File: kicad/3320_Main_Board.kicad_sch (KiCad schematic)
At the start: 53 parts, among them J5 EuroPower_JST_3P, J6 EURO_PWR_16P, U1 AS3320, U2 TL072, U3 TL074

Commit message: added pcb rev 0.1.0
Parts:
- R1, R10, R11, R12, R13, R14, R15, R16, R17, R18, R19, R2, R20, R21, R22, R23, R24, R25, R26, R27, R28, R29, R3, R30, R31, R4, R5, R6, R7, R8, R9: footprint DIYSynthMNL:R_quarter_watt_L6.3mm_D2.5mm_P7.62mm -> Resistor_THT:R_Axial_DIN0207_L6.3mm_D2.5mm_P2.54mm_Vertical

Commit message: updated pcb revision 0.1.0
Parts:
- added H1: MountingHole_Pad, DIYSynthMNL:MountingHole_M3_Standoff_Pad, symbol Mechanical:MountingHole_Pad
- C12, C9: footprint DIYSynthMNL:CP_Radial_D4.0mm_P1.50mm -> DIYSynthMNL:CP_Radial_D5.0mm_P2.50mm
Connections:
- net GND: now also H1.1
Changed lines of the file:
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@@
       (effects (font (size 1.27 1.27)) (justify left))
     )
-    (property "Footprint" "DIYSynthMNL:CP_Radial_D4.0mm_P1.50mm" (at 117.1702 262.89 0)
+    (property "Footprint" "DIYSynthMNL:CP_Radial_D5.0mm_P2.50mm" (at 117.1702 262.89 0)
       (effects (font (size 1.27 1.27)) hide)
     )
@@
         (path "/03f11930-f7c0-4ced-9742-79790ca3496b/6be4c3d1-05b5-4b24-bcf9-a639c6a20d54"
           (reference "R25") (unit 1)
+        )
+      )
+    )
+  )
+  (symbol (lib_id "Mechanical:MountingHole_Pad") (at 285.75 228.6 0) (unit 1)
+    (in_bom yes) (on_board yes) (dnp no) (fields_autoplaced)
+    (property "Reference" "H1" (at 288.29 226.06 0)
+      (effects (font (size 1.27 1.27)) (justify left))
+    )
+    (property "Value" "MountingHole_Pad" (at 288.29 228.6 0)
+      (effects (font (size 1.27 1.27)) (justify left))
+    )
+    (property "Footprint" "DIYSynthMNL:MountingHole_M3_Standoff_Pad" (at 285.75 228.6 0)
+      (effects (font (size 1.27 1.27)) hide)
+    )
+    (property "Datasheet" "~" (at 285.75 228.6 0)
+      (effects (font (size 1.27 1.27)) hide)
+    )
+    (pin "1")
+    (instances
+      (project "3320-VCF"
+        (path "/03f11930-f7c0-4ced-9742-79790ca3496b/6be4c3d1-05b5-4b24-bcf9-a639c6a20d54"
+          (reference "H1") (unit 1)
         )
       )
@@
       (effects (font (size 1.27 1.27)) (justify left))
     )
-    (property "Footprint" "DIYSynthMNL:CP_Radial_D4.0mm_P1.50mm" (at 117.1702 255.27 0)
+    (property "Footprint" "DIYSynthMNL:CP_Radial_D5.0mm_P2.50mm" (at 117.1702 255.27 0)
       (effects (font (size 1.27 1.27)) hide)
     )
@@
         )
       )
+      (project "Electric Druid VCDO1"
+        (path "/1a79e409-2950-446e-9b6e-16f6bf0a888d/940513db-8445-4e70-8397-130f22045b59"
+          (reference "#PWR?") (unit 1)
+        )
+        (path "/1a79e409-2950-446e-9b6e-16f6bf0a888d"
+          (reference "#PWR?") (unit 1)
+        )
+      )
+      (project "3340-VCO"
+        (path "/aedb3b78-1db1-4bb8-b4e7-c509f764608a"
+          (reference "#PWR?") (unit 1)
+        )
+      )
+    )
+  )
+  (symbol (lib_id "power:GND") (at 285.75 231.14 0) (unit 1)
+    (in_bom yes) (on_board yes) (dnp no) (fields_autoplaced)
+    (property "Reference" "#PWR034" (at 285.75 237.49 0)
+      (effects (font (size 1.27 1.27)) hide)
+    )
+    (property "Value" "GND" (at 285.75 235.585 0)
+      (effects (font (size 1.27 1.27)))
+    )
+    (property "Footprint" "" (at 285.75 231.14 0)
+      (effects (font (size 1.27 1.27)) hide)
+    )
+    (property "Datasheet" "" (at 285.75 231.14 0)
+      (effects (font (size 1.27 1.27)) hide)
+    )
+    (pin "1")
+    (instances
+      (project "3320-VCF"
+        (path "/03f11930-f7c0-4ced-9742-79790ca3496b"
+          (reference "#PWR034") (unit 1)
+        )
+        (path "/03f11930-f7c0-4ced-9742-79790ca3496b/6be4c3d1-05b5-4b24-bcf9-a639c6a20d54"
+          (reference "#PWR01") (unit 1)
+        )
+      )

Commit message: updated pcb rev 0.1.0
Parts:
- U1: footprint DIYSynthMNL:DIP-18_W7.62mm_LongPads -> Package_DIP:DIP-18_W7.62mm_Socket_LongPads
- U2: footprint DIYSynthMNL:DIP-8_W7.62mm_LongPads -> Package_DIP:DIP-8_W7.62mm_Socket_LongPads
- U3: footprint DIYSynthMNL:DIP-14_W7.62mm_LongPads -> Package_DIP:DIP-14_W7.62mm_Socket_LongPads
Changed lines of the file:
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@@
       (effects (font (size 1.27 1.27)))
     )
-    (property "Footprint" "DIYSynthMNL:DIP-8_W7.62mm_LongPads" (at 295.8592 65.024 0)
+    (property "Footprint" "Package_DIP:DIP-8_W7.62mm_Socket_LongPads" (at 295.8592 65.024 0)
       (effects (font (size 1.27 1.27)) hide)
     )
@@
       (effects (font (size 1.27 1.27)))
     )
-    (property "Footprint" "DIYSynthMNL:DIP-14_W7.62mm_LongPads" (at 89.8652 207.3148 0)
+    (property "Footprint" "Package_DIP:DIP-14_W7.62mm_Socket_LongPads" (at 89.8652 207.3148 0)
       (effects (font (size 1.27 1.27)) hide)
     )
@@
       (effects (font (size 1.27 1.27)))
     )
-    (property "Footprint" "DIYSynthMNL:DIP-14_W7.62mm_LongPads" (at 200.9902 263.652 0)
+    (property "Footprint" "Package_DIP:DIP-14_W7.62mm_Socket_LongPads" (at 200.9902 263.652 0)
       (effects (font (size 1.27 1.27)) hide)
     )
@@
       (effects (font (size 1.27 1.27)))
     )
-    (property "Footprint" "DIYSynthMNL:DIP-8_W7.62mm_LongPads" (at 137.1092 62.484 0)
+    (property "Footprint" "Package_DIP:DIP-8_W7.62mm_Socket_LongPads" (at 137.1092 62.484 0)
       (effects (font (size 1.27 1.27)) hide)
     )
@@
       (effects (font (size 1.27 1.27)))
     )
-    (property "Footprint" "DIYSynthMNL:DIP-18_W7.62mm_LongPads" (at 194.2592 125.73 0)
+    (property "Footprint" "Package_DIP:DIP-18_W7.62mm_Socket_LongPads" (at 194.2592 125.73 0)
       (effects (font (size 1.27 1.27)) hide)
     )
@@
       (effects (font (size 1.27 1.27)) (justify left))
     )
-    (property "Footprint" "DIYSynthMNL:DIP-14_W7.62mm_LongPads" (at 148.0312 250.317 0)
+    (property "Footprint" "Package_DIP:DIP-14_W7.62mm_Socket_LongPads" (at 148.0312 250.317 0)
       (effects (font (size 1.27 1.27)) hide)
     )
@@
       (effects (font (size 1.27 1.27)) (justify left))
     )
-    (property "Footprint" "DIYSynthMNL:DIP-8_W7.62mm_LongPads" (at 138.3792 252.857 0)
+    (property "Footprint" "Package_DIP:DIP-8_W7.62mm_Socket_LongPads" (at 138.3792 252.857 0)
       (effects (font (size 1.27 1.27)) hide)
     )
@@
       (effects (font (size 1.27 1.27)))
     )
-    (property "Footprint" "DIYSynthMNL:DIP-14_W7.62mm_LongPads" (at 61.1632 204.7748 0)
+    (property "Footprint" "Package_DIP:DIP-14_W7.62mm_Socket_LongPads" (at 61.1632 204.7748 0)
       (effects (font (size 1.27 1.27)) hide)
     )
@@
       (effects (font (size 1.27 1.27)))
     )
-    (property "Footprint" "DIYSynthMNL:DIP-14_W7.62mm_LongPads" (at 70.6628 148.2852 0)
-      (effects (font (size 1.27 1.27)) hide)
-    )
+    (property "Footprint" "Package_DIP:DIP-14_W7.62mm_Socket_LongPads" (at 70.6628 148.2852 0)
+      (effects (font (size 1.27 1.27)) hide)
+    )

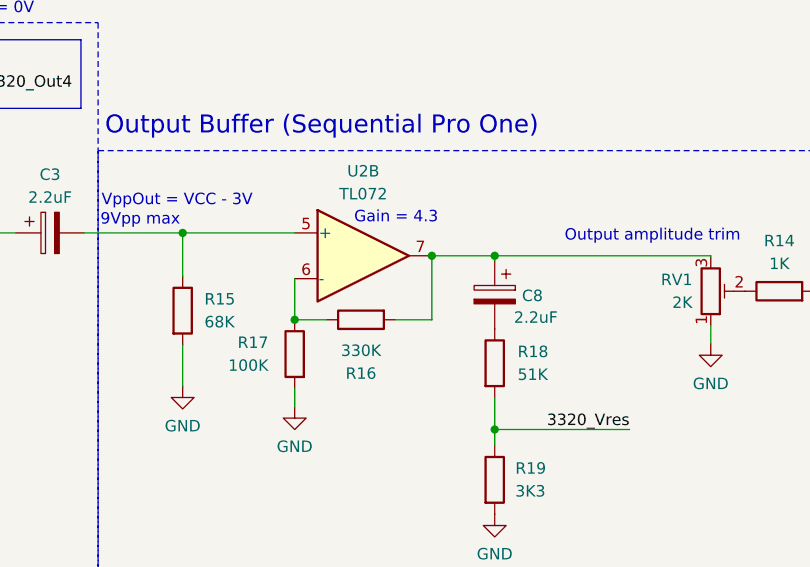
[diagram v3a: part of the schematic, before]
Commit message: Add schematic revision 0.1.5
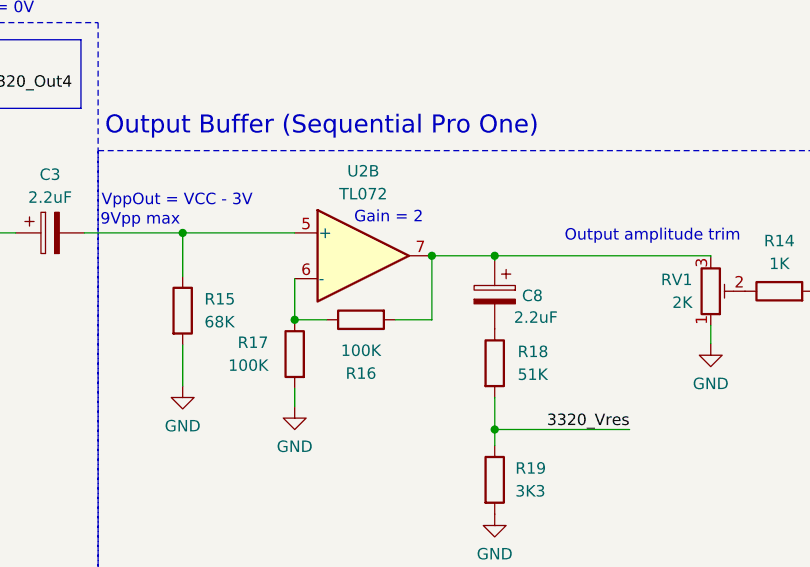
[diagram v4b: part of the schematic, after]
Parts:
- R16: value 330K -> 100K
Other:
- note added: "Gain = 2"
- note removed: "Gain = 4.3"
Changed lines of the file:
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@@
     (title "Eurorack 3320 Low Pass VCF")
     (date "2024-02-16")
-    (rev "0.1.4")
+    (rev "0.1.5")
     (company "DIYSynthMNL")
     (comment 1 "This version is a prototype")
@@
     (effects (font (size 1.27 1.27)) (justify left bottom))
   )
-  (text "Gain = 4.3" (at 294.8432 61.595 0)
+  (text "Gain = 2\n" (at 294.8432 61.595 0)
     (effects (font (size 1.27 1.27)) (justify left bottom))
   )
@@
       (effects (font (size 1.27 1.27)))
     )
-    (property "Value" "330K" (at 295.6052 75.565 90)
-      (effects (font (size 1.27 1.27)))
-    )
+    (property "Value" "100K" (at 295.6052 75.565 90)
+      (effects (font (size 1.27 1.27)))
+    )

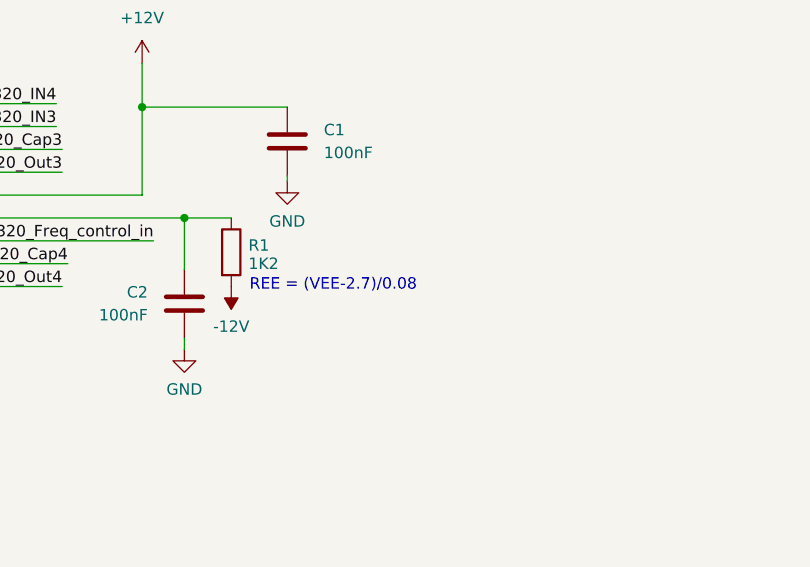
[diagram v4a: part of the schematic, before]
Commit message: fix: correct REE formula divisor in schematic comment
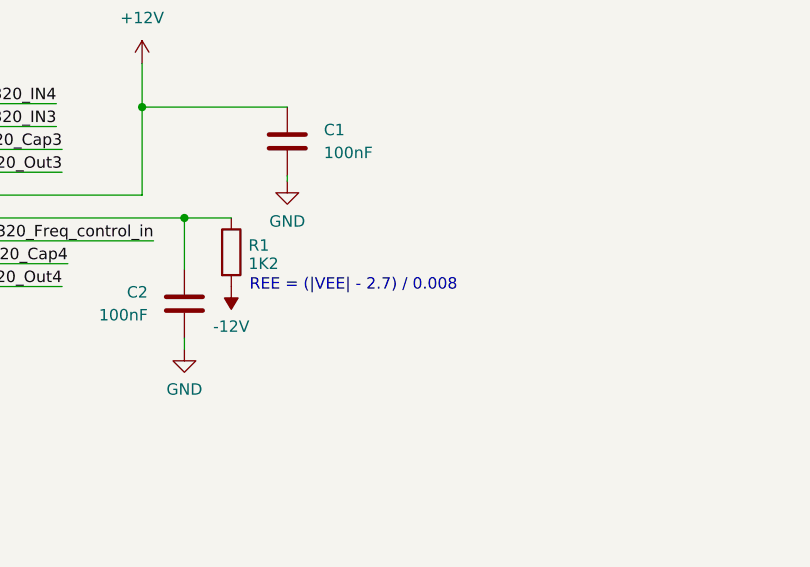
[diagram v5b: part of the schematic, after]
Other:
- note added: "REE = (|VEE| - 2.7) / 0.008"
- note removed: "REE = (VEE-2.7)/0.08"
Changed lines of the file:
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@@
     (effects (font (size 1.27 1.27)) (justify left bottom))
   )
-  (text "REE = (VEE-2.7)/0.08" (at 255.0922 150.495 0)
+  (text "REE = (|VEE| - 2.7) / 0.008" (at 255.0922 150.495 0)
     (effects (font (size 1.27 1.27)) (justify left bottom))
   )
